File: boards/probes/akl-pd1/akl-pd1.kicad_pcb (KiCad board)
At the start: 2 copper layers, 150.5 x 23.5 mm, 9 parts, among them J1 901-10511-3, J2 901-10511-3, J3 GNDSOCKET

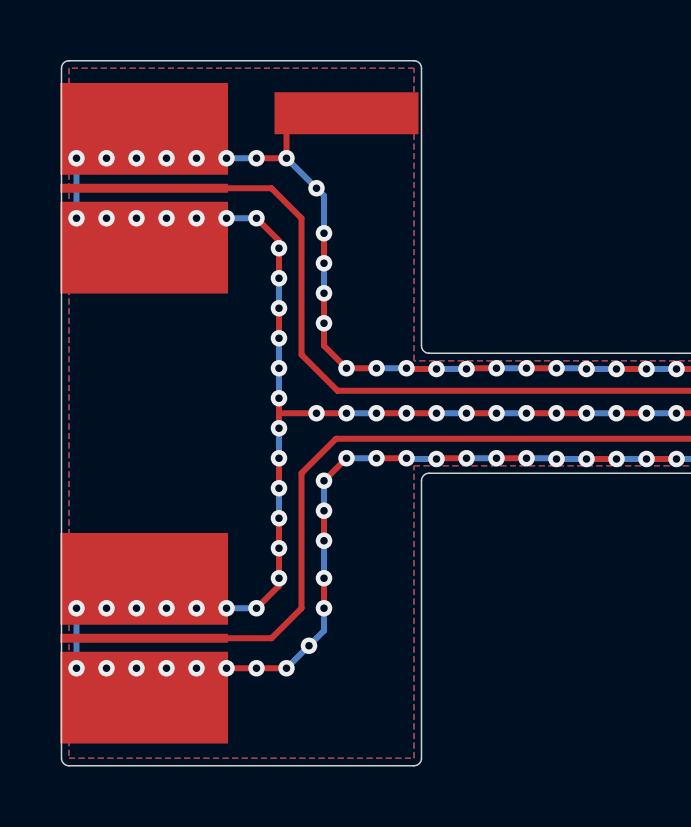
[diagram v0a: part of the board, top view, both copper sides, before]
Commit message: Updated AKL-PD1 design with SMPM
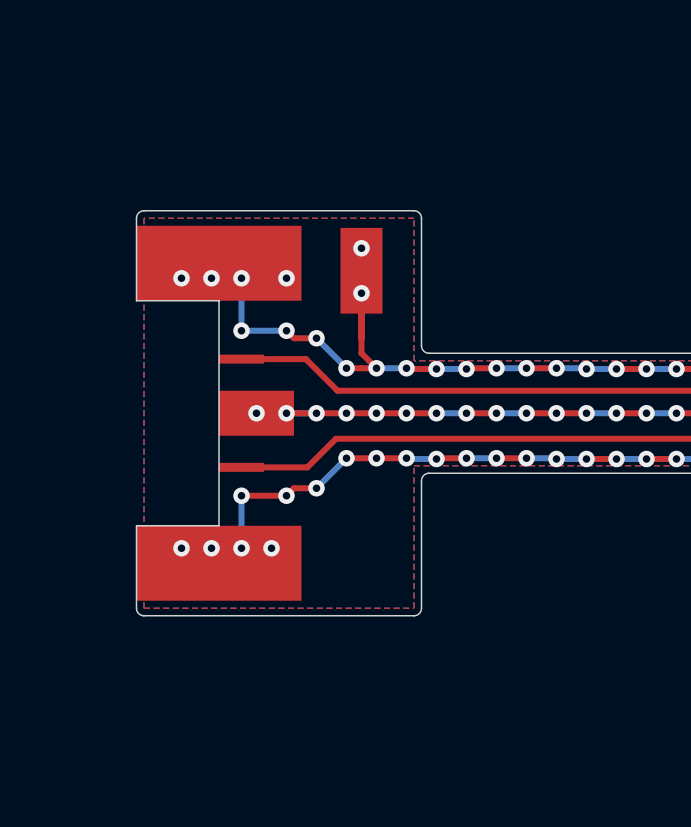
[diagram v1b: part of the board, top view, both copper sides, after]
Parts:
- removed J2: 901-10511-3, azonenberg_pcb:CONN_SMA_EDGE_AMPHENOL_901_10511_3
- J1: value 901-10511-3 -> 3211-60087; footprint azonenberg_pcb:CONN_SMA_EDGE_AMPHENOL_901_10511_3 -> azonenberg_pcb:CONN_SMPM_DUAL_AMPHENOL_3211-60087
- moved J1 7.91 mm to (55.2, 76.5)
- moved J3 5.27 mm to (60.0, 71.8), turned to 90 degrees
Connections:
- J1 pad 2: /GND -> /IN_N
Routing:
- net /GND: track 471.8 -> 438.6 mm, vias 462 -> 427
- net /IN_P: track 148.5 -> 140.2 mm
- net /IN_N: track 148.4 -> 140.2 mm
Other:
- board size 150.5 x 23.5 mm -> 148 x 13.5 mm

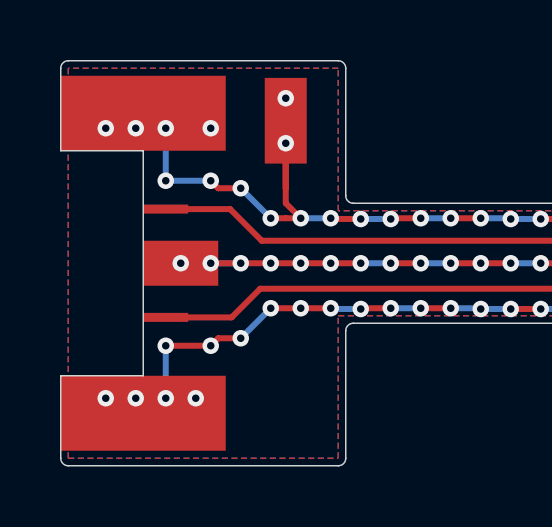
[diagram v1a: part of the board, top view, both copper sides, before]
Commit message: Final v0.1 AKL-PD1 layout for prototype
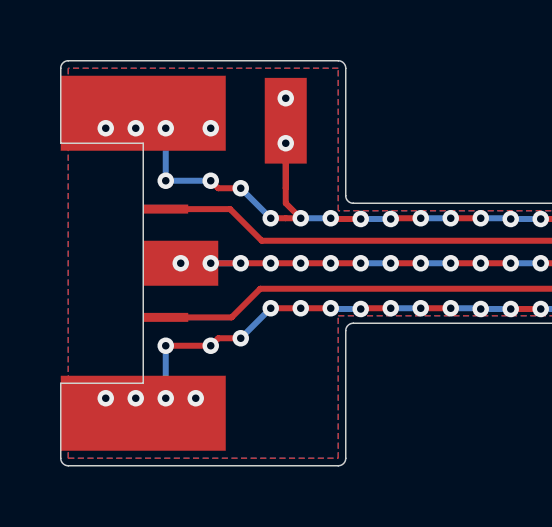
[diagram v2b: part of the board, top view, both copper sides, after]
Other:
- outline, holes or cut-outs redrawn
- board text added: "AKL-PD1 / v0.1 / A. Zonenberg / 2020-12-28"
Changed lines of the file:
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@@
   (general
     (thickness 1.6)
-    (drawings 20)
+    (drawings 21)
     (tracks 910)
     (zones 0)
@@
       (psnegative false)
       (psa4output false)
-      (plotreference true)
-      (plotvalue true)
+      (plotreference false)
+      (plotvalue false)
       (plotinvisibletext false)
       (padsonsilk false)
@@
       (outputformat 1)
       (mirror false)
-      (drillshape 1)
+      (drillshape 0)
       (scaleselection 1)
-      (outputdirectory ""))
+      (outputdirectory "output/"))
   )
   (net 0 "")
@@
     )
   )
-  (gr_line (start 52.5 72.75) (end 52.5 70) (layer Edge.Cuts) (width 0.05))
-  (gr_line (start 55.25 72.75) (end 52.5 72.75) (layer Edge.Cuts) (width 0.05))
-  (gr_line (start 55.25 80.25) (end 55.25 72.75) (layer Edge.Cuts) (width 0.05))
-  (gr_line (start 52.5 80.25) (end 55.25 80.25) (layer Edge.Cuts) (width 0.05))
-  (gr_line (start 52.5 83) (end 52.5 80.25) (layer Edge.Cuts) (width 0.05))
+  (gr_text "AKL-PD1 / v0.1 / A. Zonenberg / 2020-12-28" (at 175.5 75.75) (layer B.SilkS)
+    (effects (font (size 1 1) (thickness 0.15)) (justify mirror))
+  )
+  (gr_line (start 52.5 72.5) (end 52.5 70) (layer Edge.Cuts) (width 0.05))
+  (gr_line (start 55.25 72.5) (end 52.5 72.5) (layer Edge.Cuts) (width 0.05))
+  (gr_line (start 55.25 80.5) (end 55.25 72.5) (layer Edge.Cuts) (width 0.05))
+  (gr_line (start 52.5 80.5) (end 55.25 80.5) (layer Edge.Cuts) (width 0.05))
+  (gr_line (start 52.5 83) (end 52.5 80.5) (layer Edge.Cuts) (width 0.05))
   (gr_arc (start 52.75 70) (end 52.75 69.75) (angle -90) (layer Edge.Cuts) (width 0.05))
   (gr_line (start 61.75 83.25) (end 52.75 83.25) (layer Edge.Cuts) (width 0.05))
